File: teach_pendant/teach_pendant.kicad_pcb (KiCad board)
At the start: 2 copper layers, 171.1 x 70.8 mm, 11 parts, among them J1 Screw_Terminal_01x04, J2 KY-023, J3 KY-023, SW1 SW_Push, SW2 SW_Push, U1 ESP32-DEVKITC-32D, U2 TFT_ILI9488

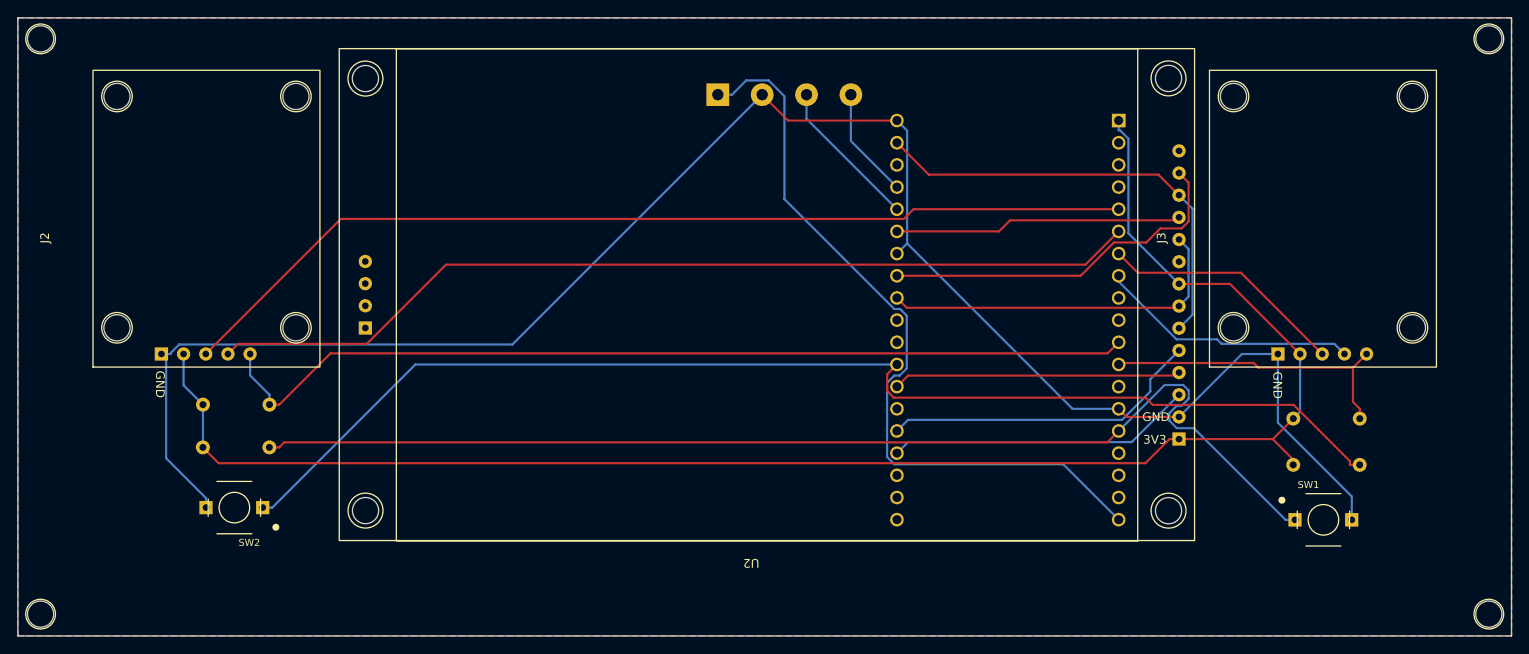
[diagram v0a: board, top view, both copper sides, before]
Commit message: agrego funcion boton de paro y librerias necesarias
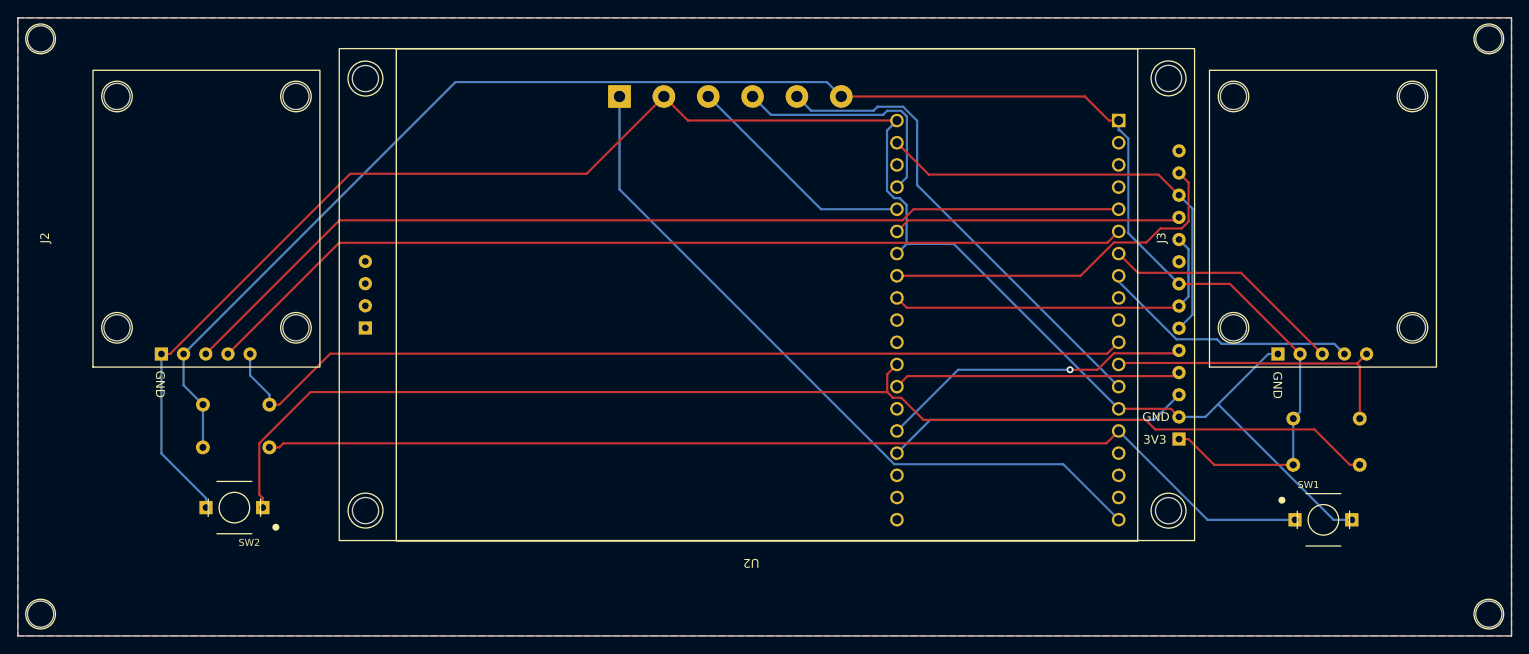
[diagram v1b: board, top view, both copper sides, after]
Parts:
- J1: footprint TerminalBlock_Phoenix:TerminalBlock_Phoenix_MKDS-1,5-4-5.08_1x04_P5.08mm_Horizontal -> TerminalBlock_Phoenix:TerminalBlock_Phoenix_MKDS-1,5-6-5.08_1x06_P5.08mm_Horizontal
- moved J1 11.3 mm to (138.8, 38.6)
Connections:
- U1 pad J2-13: unconnected-(U1-IO12-PadJ2-13) -> EMO0
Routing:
- net EMO0: track 0.00 -> 55.3 mm
- net TX: track 12.8 -> 27.6 mm
- net SW1: track 132.3 -> 122.5 mm
- net 3V3: track 189.9 -> 199.6 mm
- net RX: track 17.4 -> 27.0 mm
- net 5V: track 87.4 -> 83.5 mm
- net SW2: track 140.8 -> 143.1 mm
- net DC/RS: track 37.0 -> 36.1 mm, vias 0 -> 1
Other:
- board text added: "EMO"
